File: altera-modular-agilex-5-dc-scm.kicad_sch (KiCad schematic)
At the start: 0 parts

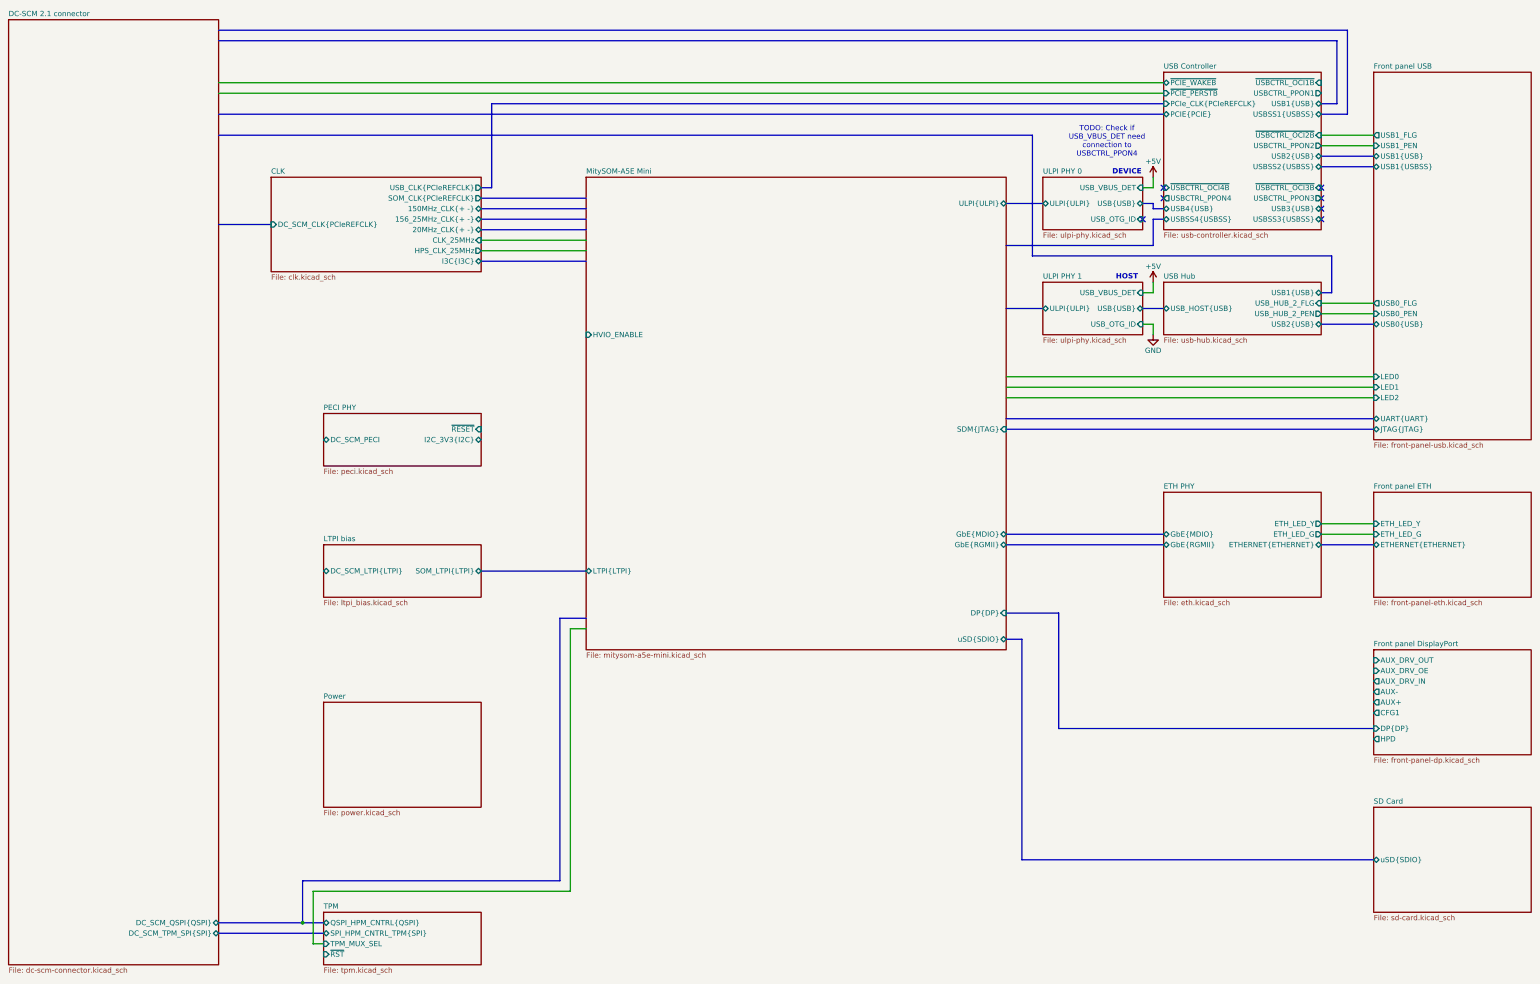
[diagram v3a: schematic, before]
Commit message: [#99974] Import DC-SCM ports on root schematic, start connecting them to other blocks
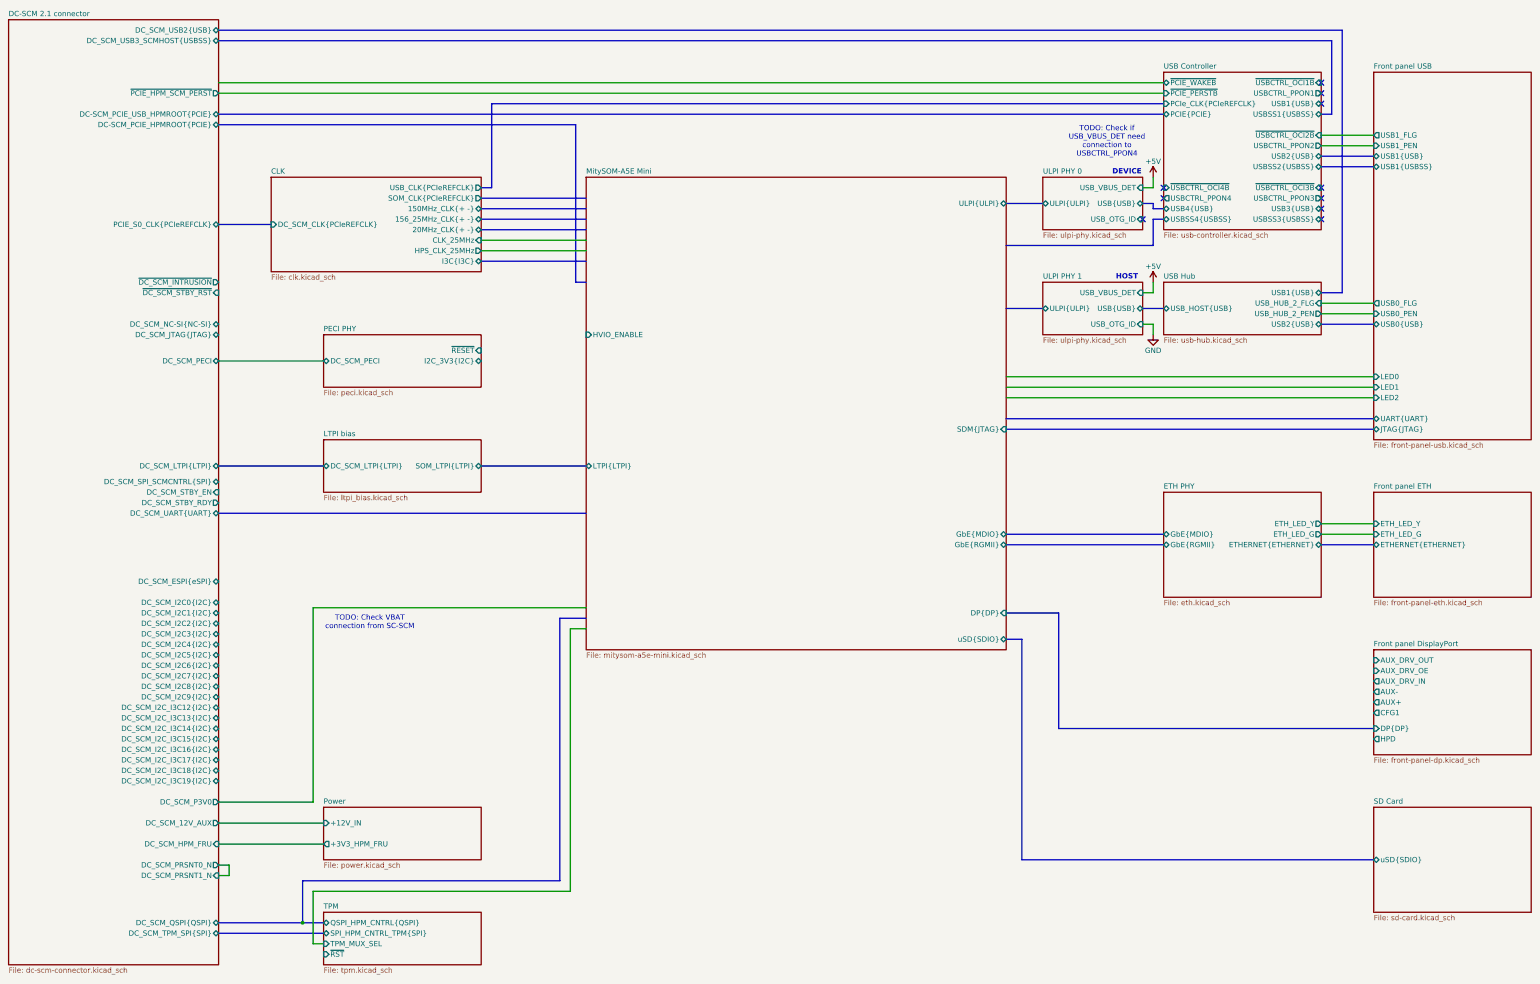
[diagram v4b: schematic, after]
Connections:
- no-connect marks 7 -> 10
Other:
- sheet DC-SCM 2.1 connector ports: added DC-SCM_PCIE_HPMROOT{PCIE}, DC-SCM_PCIE_USB_HPMROOT{PCIE}, DC_SCM_12V_AUX, DC_SCM_ESPI{eSPI}, DC_SCM_HPM_FRU, DC_SCM_I2C0{I2C}, DC_SCM_I2C1{I2C}, DC_SCM_I2C2{I2C}, DC_SCM_I2C3{I2C}, DC_SCM_I2C4{I2C}, DC_SCM_I2C5{I2C}, DC_SCM_I2C6{I2C}, DC_SCM_I2C7{I2C}, DC_SCM_I2C8{I2C}, DC_SCM_I2C9{I2C}, DC_SCM_I2C_I3C12{I2C}, DC_SCM_I2C_I3C13{I2C}, DC_SCM_I2C_I3C14{I2C}, DC_SCM_I2C_I3C15{I2C}, DC_SCM_I2C_I3C16{I2C}, DC_SCM_I2C_I3C17{I2C}, DC_SCM_I2C_I3C18{I2C}, DC_SCM_I2C_I3C19{I2C}, DC_SCM_JTAG{JTAG}, DC_SCM_LTPI{LTPI}, DC_SCM_NC-SI{NC-SI}, DC_SCM_P3V0, DC_SCM_PECI, DC_SCM_PRSNT0_N, DC_SCM_PRSNT1_N, DC_SCM_SPI_SCMCNTRL{SPI}, DC_SCM_STBY_EN, DC_SCM_STBY_RDY, DC_SCM_UART{UART}, DC_SCM_USB2{USB}, DC_SCM_USB3_SCMHOST{USBSS}, PCIE_S0_CLK{PCIeREFCLK}, ~{DC_SCM_INTRUSION}, ~{DC_SCM_STBY_RST}, ~{PCIE_HPM_SCM_PERST}; removed none
- sheet Power ports: added +12V_IN, +3V3_HPM_FRU; removed none
- note added: "TODO: Check VBAT connection from SC-SCM"

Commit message: [#99974] Connect remaining DC-SCM signals on root schematic, except for I2C
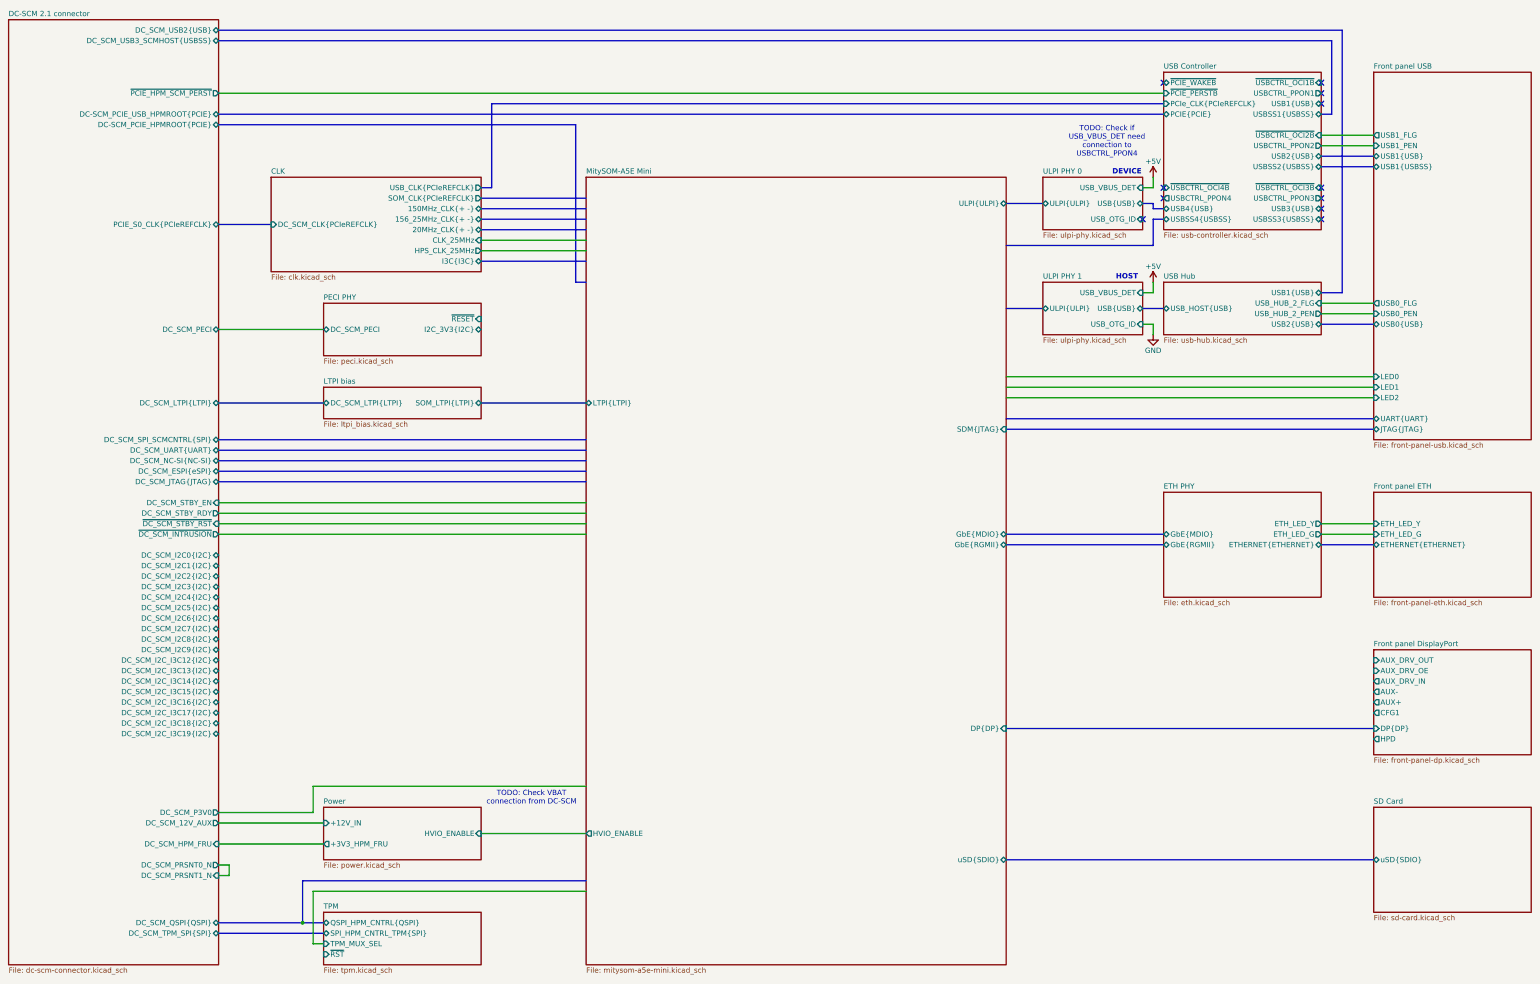
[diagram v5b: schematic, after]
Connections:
- no-connect marks 10 -> 11
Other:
- sheet Power ports: added HVIO_ENABLE; removed none
- note added: "TODO: Check VBAT connection from DC-SCM"
- note removed: "TODO: Check VBAT connection from SC-SCM"

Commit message: [#100060] Add and connect high speed connector
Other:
- sheet MitySOM-A5E Mini ports: added 20MHz_CLK{+ -}, AUX+, AUX-, AUX_DRV_IN, AUX_DRV_OE, AUX_DRV_OUT, CFG1, DC-SCM_PCIE_USB_SCMROOT{PCIE}, HPD, USBSS4{USBSS}; removed none
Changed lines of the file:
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@@
+		)
+	)
+	(wire
+		(pts
+			(xy 266.7 182.88) (xy 355.6 182.88)
+		)
+		(stroke
+			(width 0)
+			(type default)
 		)
 	)
@@
 		)
 	)
+	(wire
+		(pts
+			(xy 266.7 180.34) (xy 355.6 180.34)
+		)
+		(stroke
+			(width 0)
+			(type default)
+		)
+	)
 	(bus
 		(pts
@@
 		)
 	)
+	(wire
+		(pts
+			(xy 266.7 185.42) (xy 355.6 185.42)
+		)
+		(stroke
+			(width 0)
+			(type default)
+		)
+	)
 	(bus
 		(pts
@@
 		)
 	)
+	(wire
+		(pts
+			(xy 266.7 199.39) (xy 355.6 199.39)
+		)
+		(stroke
+			(width 0)
+			(type default)
+		)
+	)
 	(bus
 		(pts
@@
 	(wire
 		(pts
+			(xy 266.7 190.5) (xy 355.6 190.5)
+		)
+		(stroke
+			(width 0)
+			(type default)
+		)
+	)
+	(wire
+		(pts
 			(xy 342.9 147.32) (xy 355.6 147.32)
 		)
@@
 		)
 	)
+	(wire
+		(pts
+			(xy 266.7 193.04) (xy 355.6 193.04)
+		)
+		(stroke
+			(width 0)
+			(type default)
+		)
+	)
 	(bus
 		(pts
@@
 		(pts
 			(xy 99.06 236.22) (xy 99.06 248.92)
+		)
+		(stroke
+			(width 0)
+			(type default)
+		)
+	)
+	(wire
+		(pts
+			(xy 266.7 187.96) (xy 355.6 187.96)
 		)
 		(stroke
@@
 			)
 		)
+		(pin "DC-SCM_PCIE_USB_SCMROOT{PCIE}" bidirectional
+			(at 165.1 101.6 180)
+			(effects
+				(font
+					(size 1.27 1.27)
+				)
+				(justify left)
+			)
+		)
+		(pin "USBSS4{USBSS}" bidirectional
+			(at 266.7 80.01 0)
+			(effects
+				(font
+					(size 1.27 1.27)
+				)
+				(justify right)
+			)
+		)
+		(pin "20MHz_CLK{+ -}" bidirectional
+			(at 165.1 76.2 180)
+			(effects
+				(font
+					(size 1.27 1.27)
+				)
+				(justify left)
+			)
+		)
+		(pin "AUX-" output
+			(at 266.7 187.96 0)
+			(effects
+				(font
+					(size 1.27 1.27)
+				)
+				(justify right)
+			)
+		)
+		(pin "AUX+" output
+			(at 266.7 190.5 0)
+			(effects
+				(font
+					(size 1.27 1.27)
+				)
+				(justify right)
+			)
+		)
+		(pin "AUX_DRV_IN" output
+			(at 266.7 185.42 0)
+			(effects
+				(font
+					(size 1.27 1.27)
+				)
+				(justify right)
+			)
+		)
+		(pin "AUX_DRV_OUT" input
+			(at 266.7 180.34 0)
+			(effects
+				(font
+					(size 1.27 1.27)
+				)
+				(justify right)
+			)
+		)
+		(pin "AUX_DRV_OE" input
+			(at 266.7 182.88 0)
+			(effects
+				(font
+					(size 1.27 1.27)
+				)
+				(justify right)
+			)
+		)
+		(pin "HPD" output
+			(at 266.7 199.39 0)
+			(effects
+				(font
+					(size 1.27 1.27)
+				)
+				(justify right)
+			)
+		)
+		(pin "CFG1" output
+			(at 266.7 193.04 0)
+			(effects
+				(font
+					(size 1.27 1.27)
+				)
+				(justify right)
+			)
+		)
